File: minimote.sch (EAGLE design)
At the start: 41 parts, among them IC1 ATTINY841, J1 AVR_SPI_PROG_3X2PTH, J2 EDGEUSB, P1 TOUCHPAD, P2 TOUCHPAD, P3 TOUCHPAD, P4 TOUCHPAD, P5 TOUCHPAD, P6 TOUCHPAD, P7 TOUCHPAD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

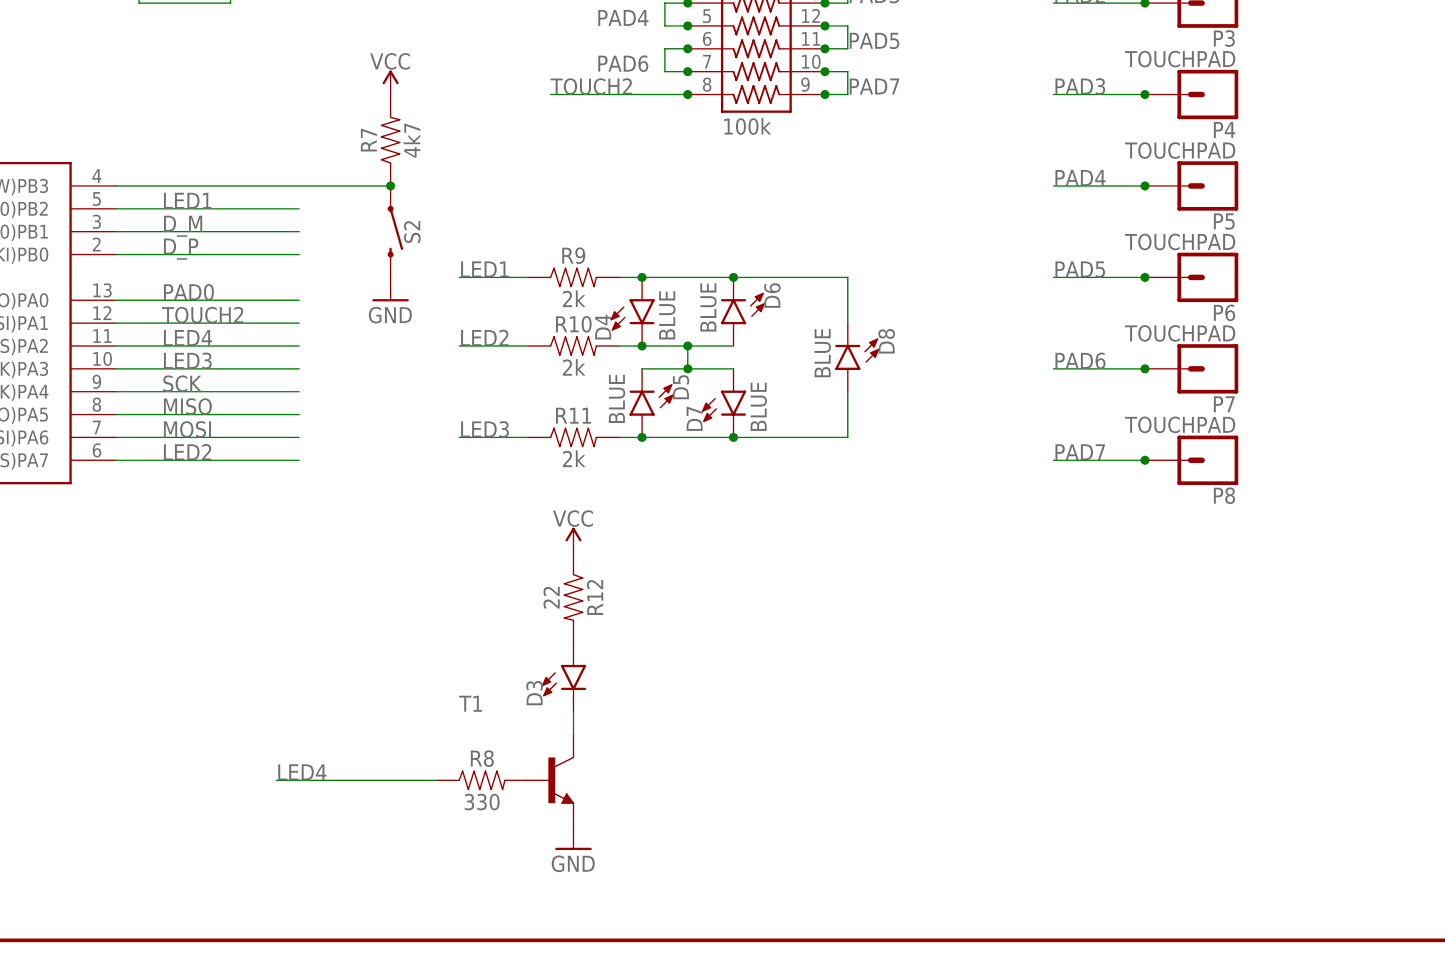
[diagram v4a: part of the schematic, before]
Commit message: added footprint for i2c eeprom
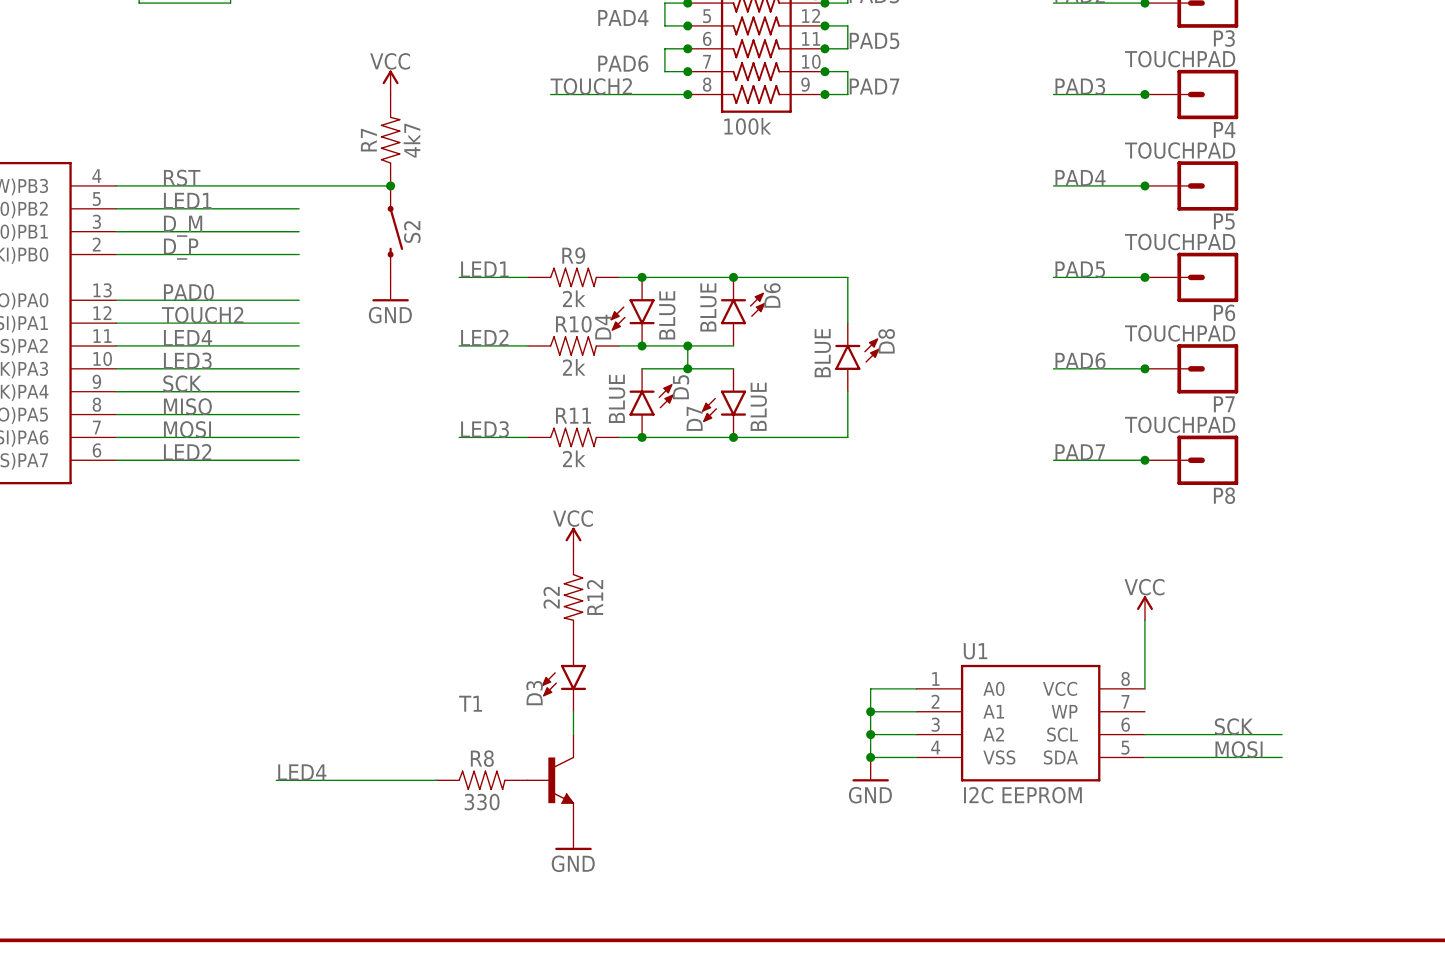
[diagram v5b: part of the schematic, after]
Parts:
- added U1: I2C EEPROM, SparkFun-IC-Memory:EEPROM-I2CEIAJ
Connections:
- removed net N$10: IC1.(PCINT11/ADC9/RESET/DW)PB3, R7.1, S2.1
- net GND: now also U1.A0, U1.A1, U1.A2, U1.VSS
- net MOSI: now also U1.SDA
- net RST: now also IC1.(PCINT11/ADC9/RESET/DW)PB3, R7.1, S2.1
- net SCK: now also U1.SCL
- net VCC: now also U1.VCC
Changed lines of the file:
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@@
 <part name="T1" library="transistor" library_urn="urn:adsk.eagle:library:402" deviceset="*-NPN-" device="SOT23-BEC" package3d_urn="urn:adsk.eagle:package:29919/2" technology="MMBT3904LT1"/>
 <part name="D3" library="minimote" deviceset="LED" device="3MM"/>
+<part name="U1" library="SparkFun-IC-Memory" library_urn="urn:adsk.eagle:library:524" deviceset="EEPROM-I2C" device="EIAJ" package3d_urn="urn:adsk.eagle:package:38842/1" value="I2C EEPROM"/>
+<part name="SUPPLY9" library="SparkFun-PowerSymbols" library_urn="urn:adsk.eagle:library:530" deviceset="VCC" device=""/>
+<part name="GND9" library="supply1" library_urn="urn:adsk.eagle:library:371" deviceset="GND" device=""/>
 </parts>
 <sheets>
@@
 <instance part="T1" gate="G$1" x="127" y="-22.86"/>
 <instance part="D3" gate="G$1" x="129.54" y="-10.16"/>
+<instance part="U1" gate="G$1" x="180.34" y="-17.78"/>
+<instance part="SUPPLY9" gate="G$1" x="193.04" y="-5.08"/>
+<instance part="GND9" gate="1" x="162.56" y="-22.86"/>
 </instances>
 <busses>
@@
 <pinref part="GND8" gate="1" pin="GND"/>
 <pinref part="T1" gate="G$1" pin="E"/>
+</segment>
+<segment>
+<pinref part="U1" gate="G$1" pin="VSS"/>
+<pinref part="GND9" gate="1" pin="GND"/>
+<wire x1="167.64" y1="-20.32" x2="162.56" y2="-20.32" width="0.1524" layer="91"/>
+<pinref part="U1" gate="G$1" pin="A2"/>
+<wire x1="162.56" y1="-20.32" x2="162.56" y2="-17.78" width="0.1524" layer="91"/>
+<wire x1="162.56" y1="-17.78" x2="167.64" y2="-17.78" width="0.1524" layer="91"/>
+<junction x="162.56" y="-20.32"/>
+<pinref part="U1" gate="G$1" pin="A1"/>
+<wire x1="162.56" y1="-17.78" x2="162.56" y2="-15.24" width="0.1524" layer="91"/>
+<wire x1="162.56" y1="-15.24" x2="167.64" y2="-15.24" width="0.1524" layer="91"/>
+<junction x="162.56" y="-17.78"/>
+<pinref part="U1" gate="G$1" pin="A0"/>
+<wire x1="162.56" y1="-15.24" x2="162.56" y2="-12.7" width="0.1524" layer="91"/>
+<wire x1="162.56" y1="-12.7" x2="167.64" y2="-12.7" width="0.1524" layer="91"/>
+<junction x="162.56" y="-15.24"/>
 </segment>
 </net>
@@
 <pinref part="R7" gate="G$1" pin="2"/>
 </segment>
+<segment>
+<pinref part="U1" gate="G$1" pin="VCC"/>
+<wire x1="193.04" y1="-12.7" x2="193.04" y2="-5.08" width="0.1524" layer="91"/>
+<pinref part="SUPPLY9" gate="G$1" pin="VCC"/>
+</segment>
 </net>
 <net name="RST" class="0">
@@
 <label x="25.4" y="-15.24" size="1.778" layer="95"/>
 <pinref part="J1" gate="G$1" pin="5"/>
+</segment>
+<segment>
+<pinref part="S2" gate="G$1" pin="1"/>
+<pinref part="R7" gate="G$1" pin="1"/>
+<pinref part="IC1" gate="IC1" pin="(PCINT11/ADC9/RESET/DW)PB3"/>
+<wire x1="78.74" y1="43.18" x2="109.22" y2="43.18" width="0.1524" layer="91"/>
+<junction x="109.22" y="43.18"/>
+<label x="83.82" y="43.18" size="1.778" layer="95"/>
 </segment>
 </net>
@@
 <pinref part="J1" gate="G$1" pin="3"/>
 </segment>
+<segment>
+<pinref part="U1" gate="G$1" pin="SCL"/>
+<wire x1="193.04" y1="-17.78" x2="208.28" y2="-17.78" width="0.1524" layer="91"/>
+<label x="200.66" y="-17.78" size="1.778" layer="95"/>
+</segment>
 </net>
 <net name="MISO" class="0">
@@
 <label x="53.34" y="-12.7" size="1.778" layer="95"/>
 <pinref part="J1" gate="G$1" pin="4"/>
+</segment>
+<segment>
+<pinref part="U1" gate="G$1" pin="SDA"/>
+<wire x1="193.04" y1="-20.32" x2="208.28" y2="-20.32" width="0.1524" layer="91"/>
+<label x="200.66" y="-20.32" size="1.778" layer="95"/>
 </segment>
 </net>
@@
 </segment>
 </net>
-<net name="N$10" class="0">
-<segment>
-<pinref part="S2" gate="G$1" pin="1"/>
-<pinref part="R7" gate="G$1" pin="1"/>
-<pinref part="IC1" gate="IC1" pin="(PCINT11/ADC9/RESET/DW)PB3"/>
-<wire x1="78.74" y1="43.18" x2="109.22" y2="43.18" width="0.1524" layer="91"/>
-<junction x="109.22" y="43.18"/>
-</segment>
-</net>

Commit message: tidied up board layout
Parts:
- added R13, R14: 10k, SparkFun-Resistors:3.3KOHM-0603-1/10W-1%
- U1: value I2C EEPROM -> M24Cxx
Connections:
- net MOSI: now also R14.1
- net SCK: now also R13.1
- net VCC: now also R13.2, R14.2

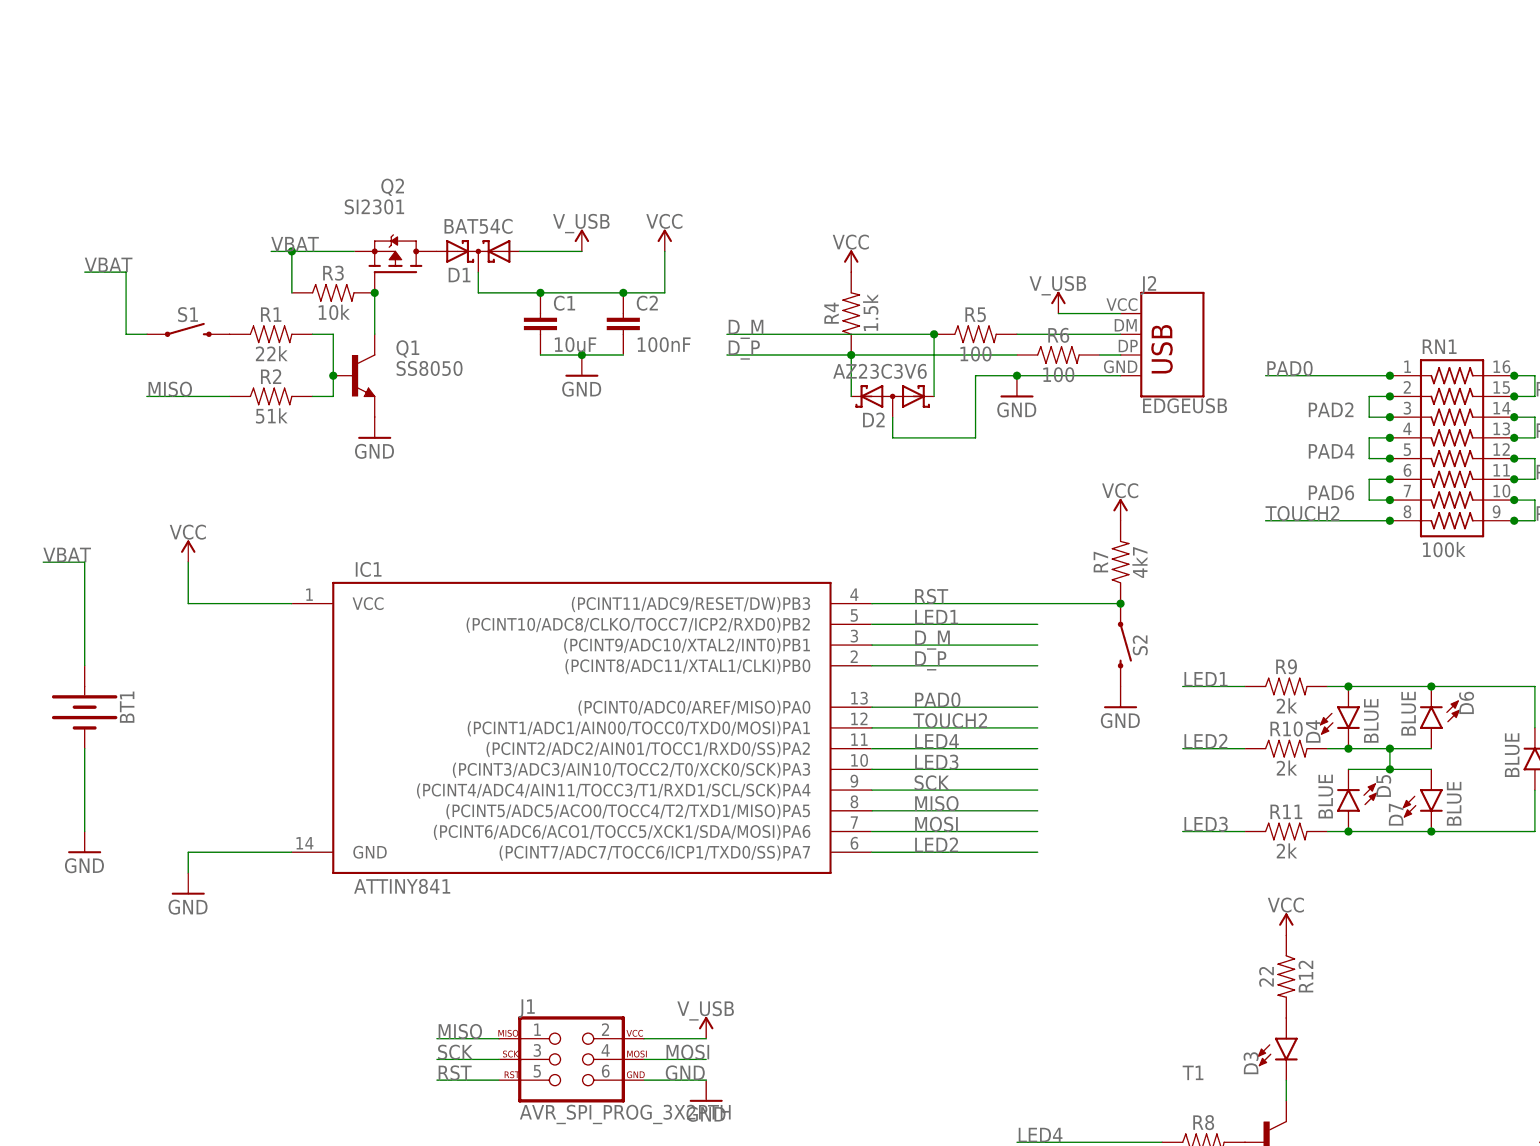
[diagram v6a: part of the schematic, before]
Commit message: Some board revisions and first firmware checkin
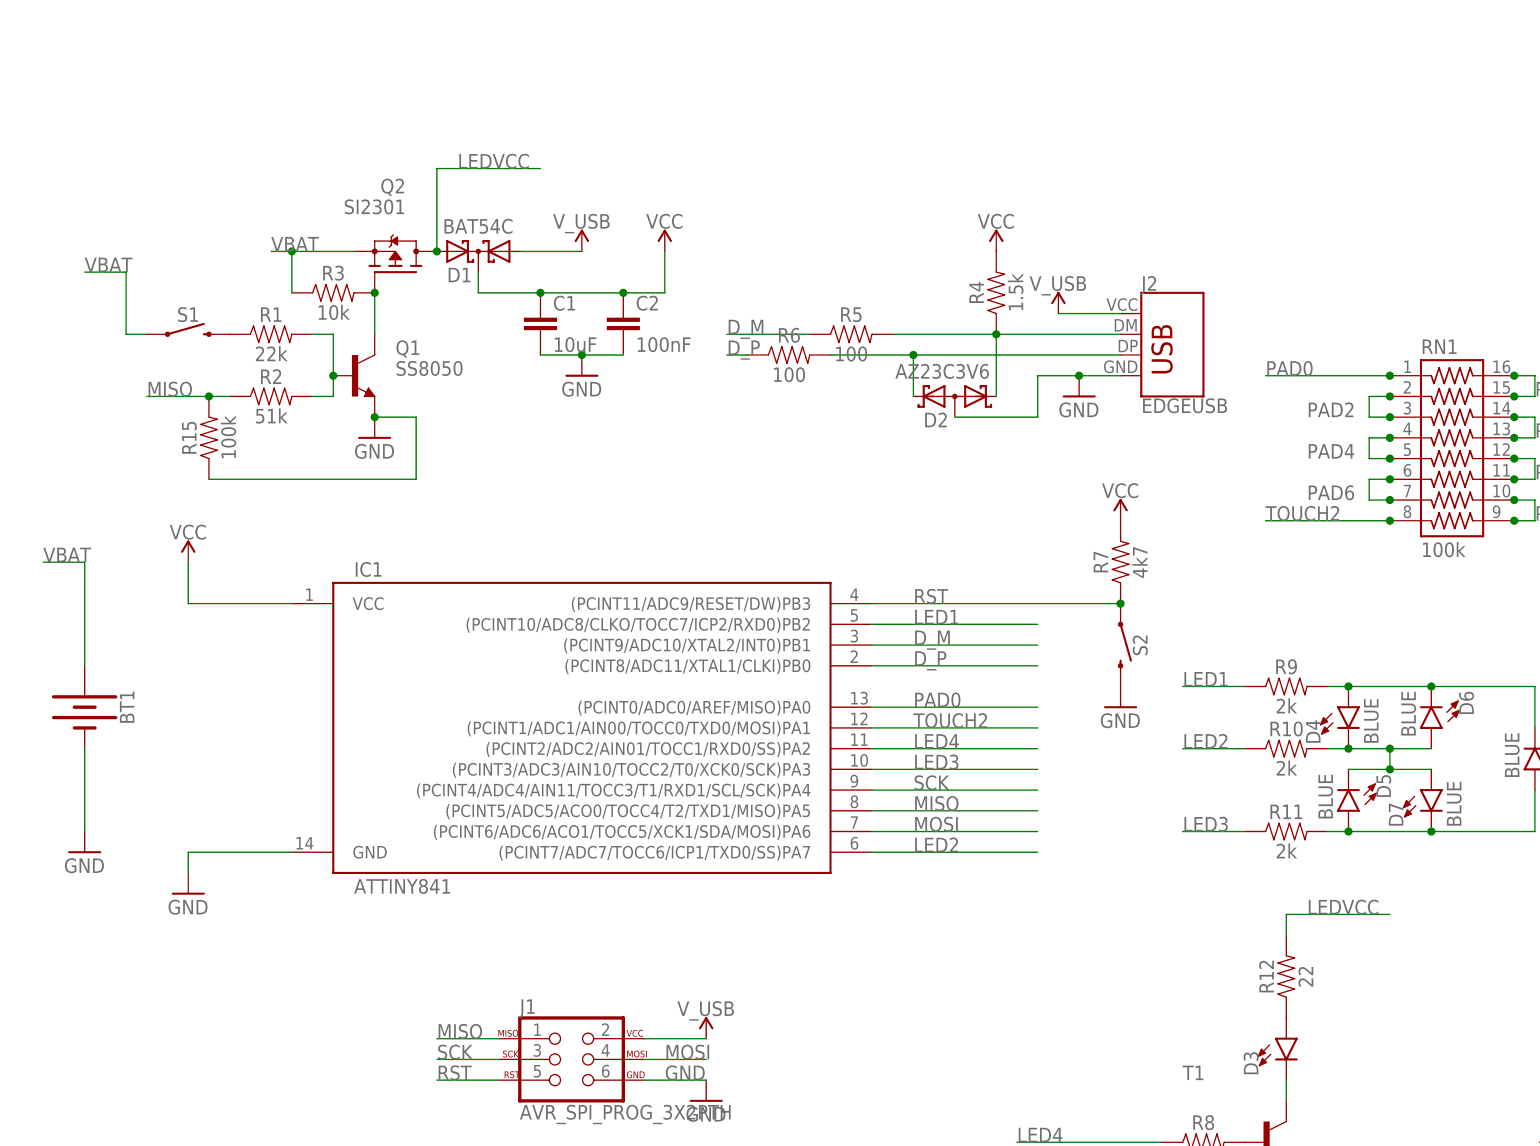
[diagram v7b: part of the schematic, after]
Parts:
- added R15: 100k, SparkFun-Resistors:3.3KOHM-0603-1/10W-1%
- R12: device SparkFun-Resistors:3.3KOHM-0603-1/10W-1% -> SparkFun-Resistors:0.22OHM-0805-1/4W-1%
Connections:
- removed net N$5: D1.A2, Q2.D
- new net LEDVCC: D1.A2, Q2.D, R12.2
- net D_M: no longer D2.K1
- net D_P: no longer D2.K2, R4.1
- net GND: now also R15.1
- net MISO: now also R15.2
- net N$1: now also R12.1; no longer R12.2
- net N$8: now also D2.K2, J2.D+, R6.2; no longer J2.D-, R5.2
- net N$9: now also D2.K1, J2.D-, R4.1, R5.2; no longer J2.D+, R6.2
- net VCC: no longer R12.1
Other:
- moved on the sheet: D2, R12, R4, R5, R6

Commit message: major pcb revisions
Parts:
- removed BT1: (no value), SparkFun-Batteries:BATTERY-20MM_SMD
- removed P1, P2, P3, P4, P5, P6, P7, P8: TOUCHPAD, minimote:TOUCHPAD
- added R16: 22M, SparkFun-Resistors:3.3KOHM-0603-1/10W-1%
- added U$1: BAT_AND_USB, minimote:BAT_AND_USB
- added U$2, U$3, U$4, U$5, U$6, U$7, U$8, U$9: BUTTON_RESISTIVE, minimote:BUTTON_RESISTIVE
- RN1: value 100k -> 10k
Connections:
- removed net PAD0: IC1.(PCINT0/ADC0/AREF/MISO)PA0, P1.1, RN1.1
- removed net TOUCH2: IC1.(PCINT1/ADC1/AIN00/TOCC0/TXD0/MOSI)PA1, RN1.8
- new net PA1: IC1.(PCINT1/ADC1/AIN00/TOCC0/TXD0/MOSI)PA1
- new net PAD_HIGH: IC1.(PCINT0/ADC0/AREF/MISO)PA0, R16.1, U$2.2, U$3.2, U$4.2, U$5.2, U$6.2, U$7.2, U$8.2, U$9.2
- net GND: now also RN1.8, U$1.-, U$2.1; no longer BT1.-
- net PAD1: now also U$3.1; no longer P2.1
- net PAD2: now also U$4.1; no longer P3.1
- net PAD3: now also U$5.1; no longer P4.1
- net PAD4: now also U$6.1; no longer P5.1
- net PAD5: now also U$7.1; no longer P6.1
- net PAD6: now also U$8.1; no longer P7.1
- net PAD7: now also U$9.1; no longer P8.1
- net VBAT: now also U$1.+; no longer BT1.+
- net VCC: now also R16.2, RN1.1
